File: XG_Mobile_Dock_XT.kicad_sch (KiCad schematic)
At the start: 45 parts, among them J1 5-1775443-8, J13 39301240, J14 I2C1, J2 20455-040E-76, J3 20455-040E-76, J5 USB_C_Receptacle, J6 455860005, J7 10147430-113T0LF, SW1 SW_Push

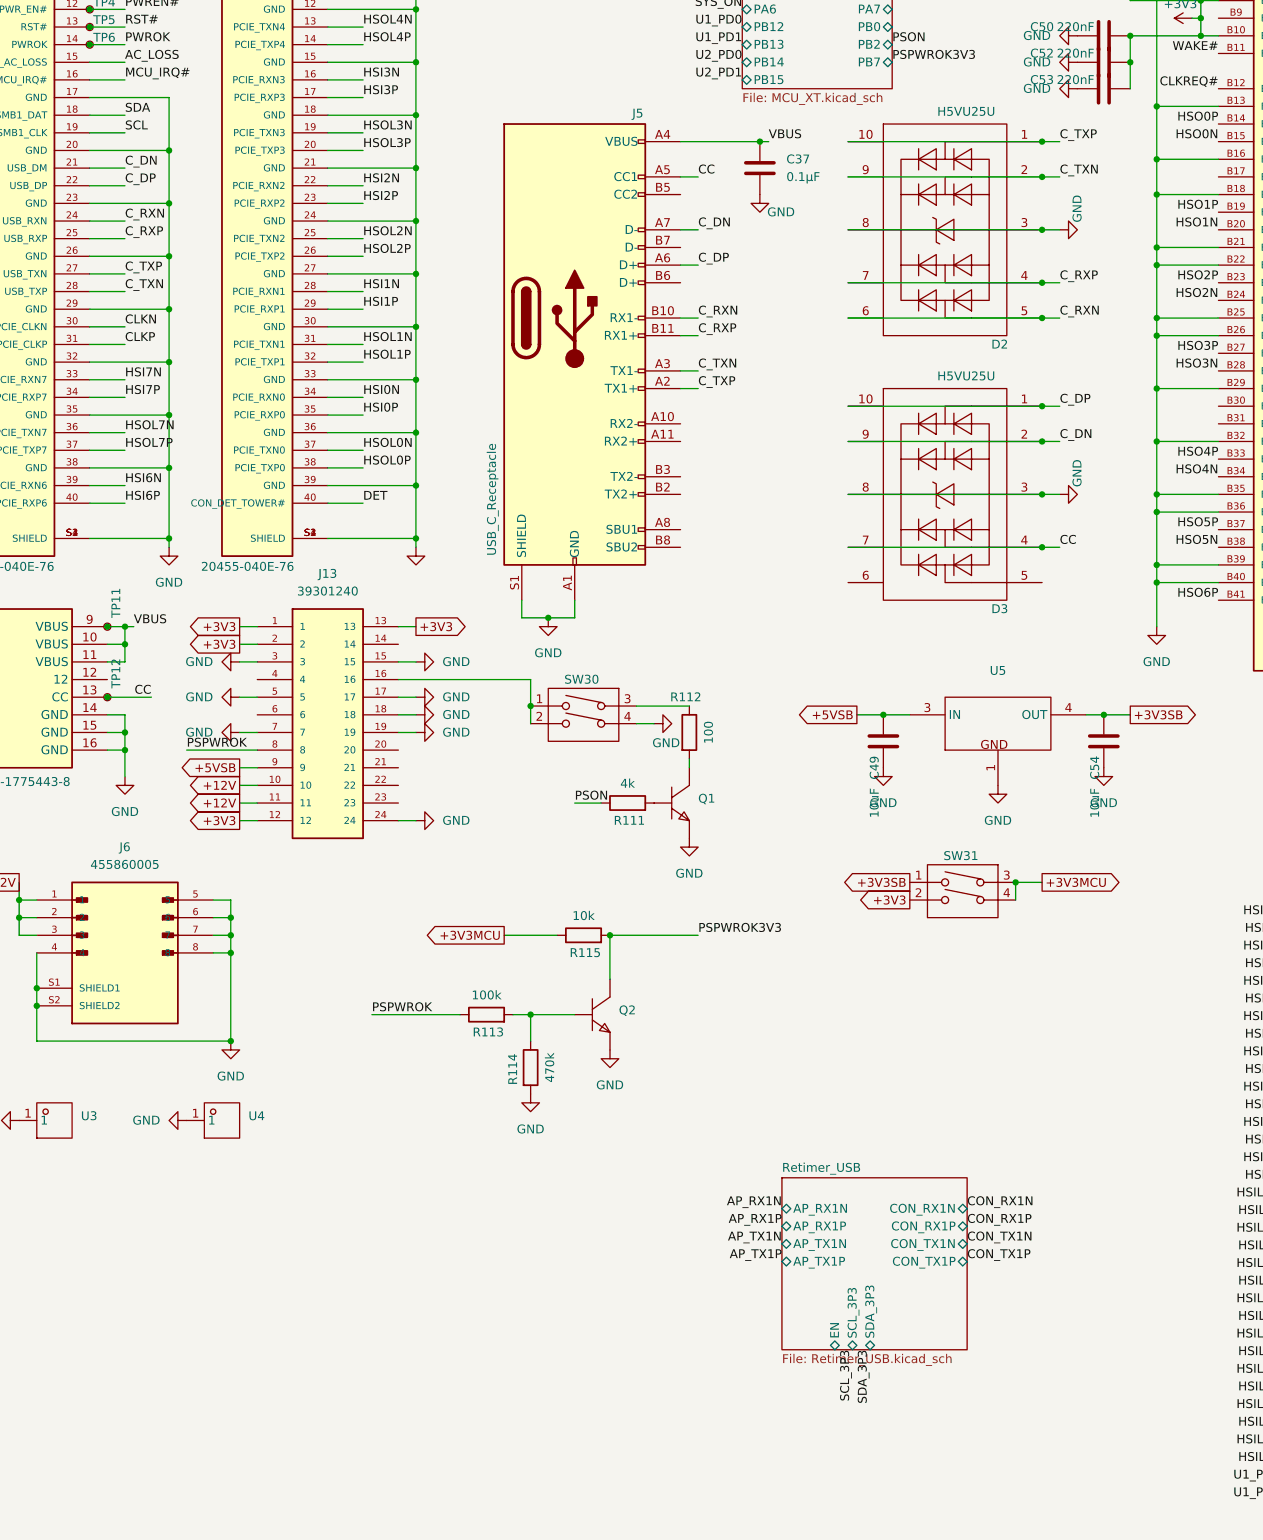
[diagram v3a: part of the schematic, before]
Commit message: almost finished adding retimer for usb
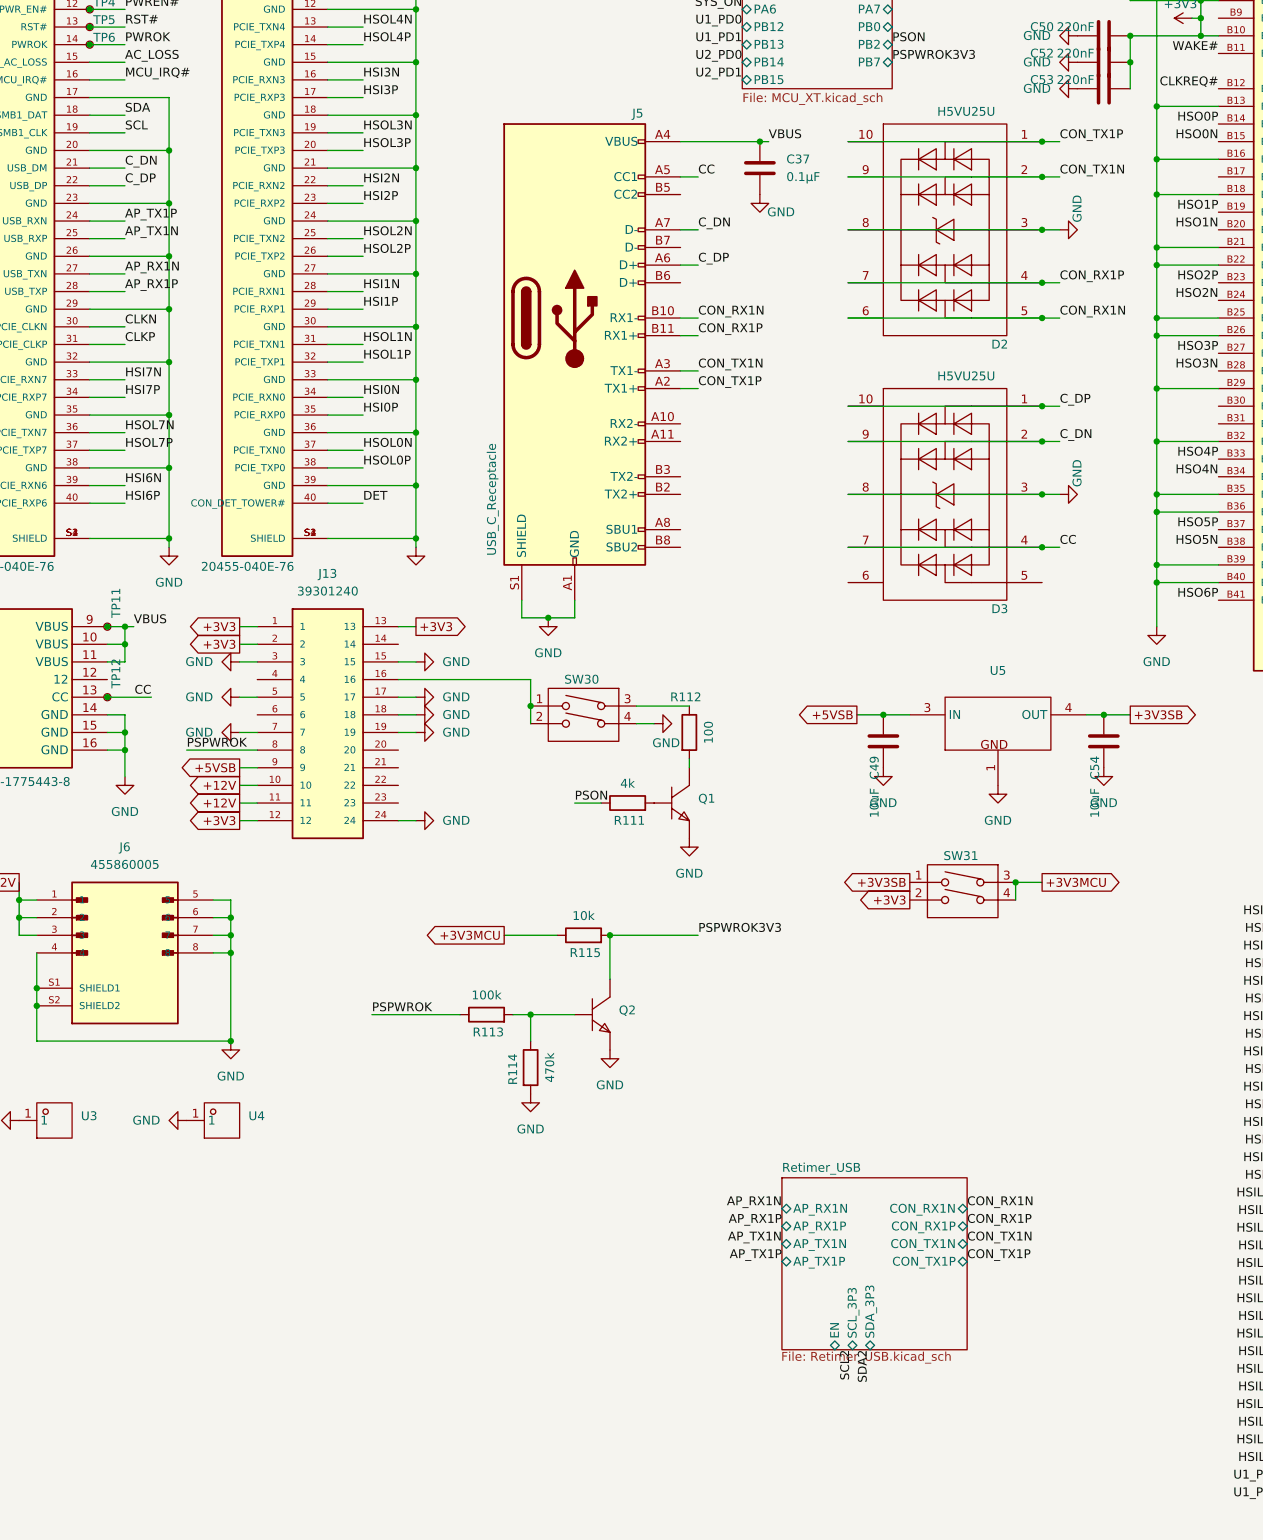
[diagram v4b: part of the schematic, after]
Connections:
- net AP_RX1N: now also J3.27 (USB_TXN)
- net AP_RX1P: now also J3.28 (USB_TXP)
- net AP_TX1N: now also J3.25 (USB_RXP)
- net AP_TX1P: now also J3.24 (USB_RXN)
- net CON_RX1N: now also D2.5 (I/O_4), D2.6 (NC), J5.B10 (RX1-)
- net CON_RX1P: now also D2.4 (I/O_3), D2.7 (NC), J5.B11 (RX1+)
- net CON_TX1N: now also D2.2 (I/O_2), D2.9 (NC), J5.A3 (TX1-)
- net CON_TX1P: now also D2.1 (I/O_1), D2.10 (NC), J5.A2 (TX1+)
- removed net C_RXN: D2.5 (I/O_4), D2.6 (NC), J3.24 (USB_RXN), J5.B10 (RX1-)
- removed net C_RXP: D2.4 (I/O_3), D2.7 (NC), J3.25 (USB_RXP), J5.B11 (RX1+)
- removed net C_TXN: D2.2 (I/O_2), D2.9 (NC), J3.28 (USB_TXP), J5.A3 (TX1-)
- removed net C_TXP: D2.1 (I/O_1), D2.10 (NC), J3.27 (USB_TXN), J5.A2 (TX1+)
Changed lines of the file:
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@@
 		)
 	)
-	(label "C_RXN"
+	(label "CON_RX1N"
 		(at 175.26 91.44 0)
 		(effects
@@
 		)
 	)
-	(label "C_RXN"
+	(label "CON_RX1N"
 		(at 123.19 91.44 0)
 		(effects
@@
 		)
 	)
-	(label "C_TXN"
+	(label "AP_RX1P"
 		(at 40.64 87.63 0)
 		(effects
@@
 		)
 	)
-	(label "C_TXP"
+	(label "CON_TX1P"
 		(at 175.26 66.04 0)
 		(effects
@@
 		)
 	)
-	(label "C_RXN"
+	(label "AP_TX1P"
 		(at 40.64 77.47 0)
 		(effects
@@
 		)
 	)
-	(label "C_RXP"
+	(label "AP_TX1N"
 		(at 40.64 80.01 0)
 		(effects
@@
 		)
 	)
-	(label "SDA_3P3"
+	(label "SDA2"
 		(at 147.955 240.03 270)
 		(effects
@@
 		)
 	)
-	(label "C_RXP"
+	(label "CON_RX1P"
 		(at 175.26 86.36 0)
 		(effects
@@
 		)
 	)
-	(label "C_TXP"
+	(label "CON_TX1P"
 		(at 123.19 101.6 0)
 		(effects
@@
 		)
 	)
-	(label "C_TXN"
+	(label "CON_TX1N"
 		(at 123.19 99.06 0)
 		(effects
@@
 		)
 	)
-	(label "C_TXN"
+	(label "CON_TX1N"
 		(at 175.26 71.12 0)
 		(effects
@@
 		)
 	)
-	(label "C_TXP"
+	(label "AP_RX1N"
 		(at 40.64 85.09 0)
 		(effects
@@
 		)
 	)
-	(label "C_RXP"
+	(label "CON_RX1P"
 		(at 123.19 93.98 0)
 		(effects
@@
 		)
 	)
-	(label "SCL_3P3"
+	(label "SCL2"
 		(at 145.415 240.03 270)
 		(effects
@@
 		(on_board yes)
 		(dnp no)
-		(fields_autoplaced yes)
 		(stroke
 			(width 0.1524)
@@
 		)
 		(property "Sheetfile" "Retimer_USB.kicad_sch"
-			(at 135.255 240.6146 0)
+			(at 135.128 240.284 0)
 			(effects
 				(font

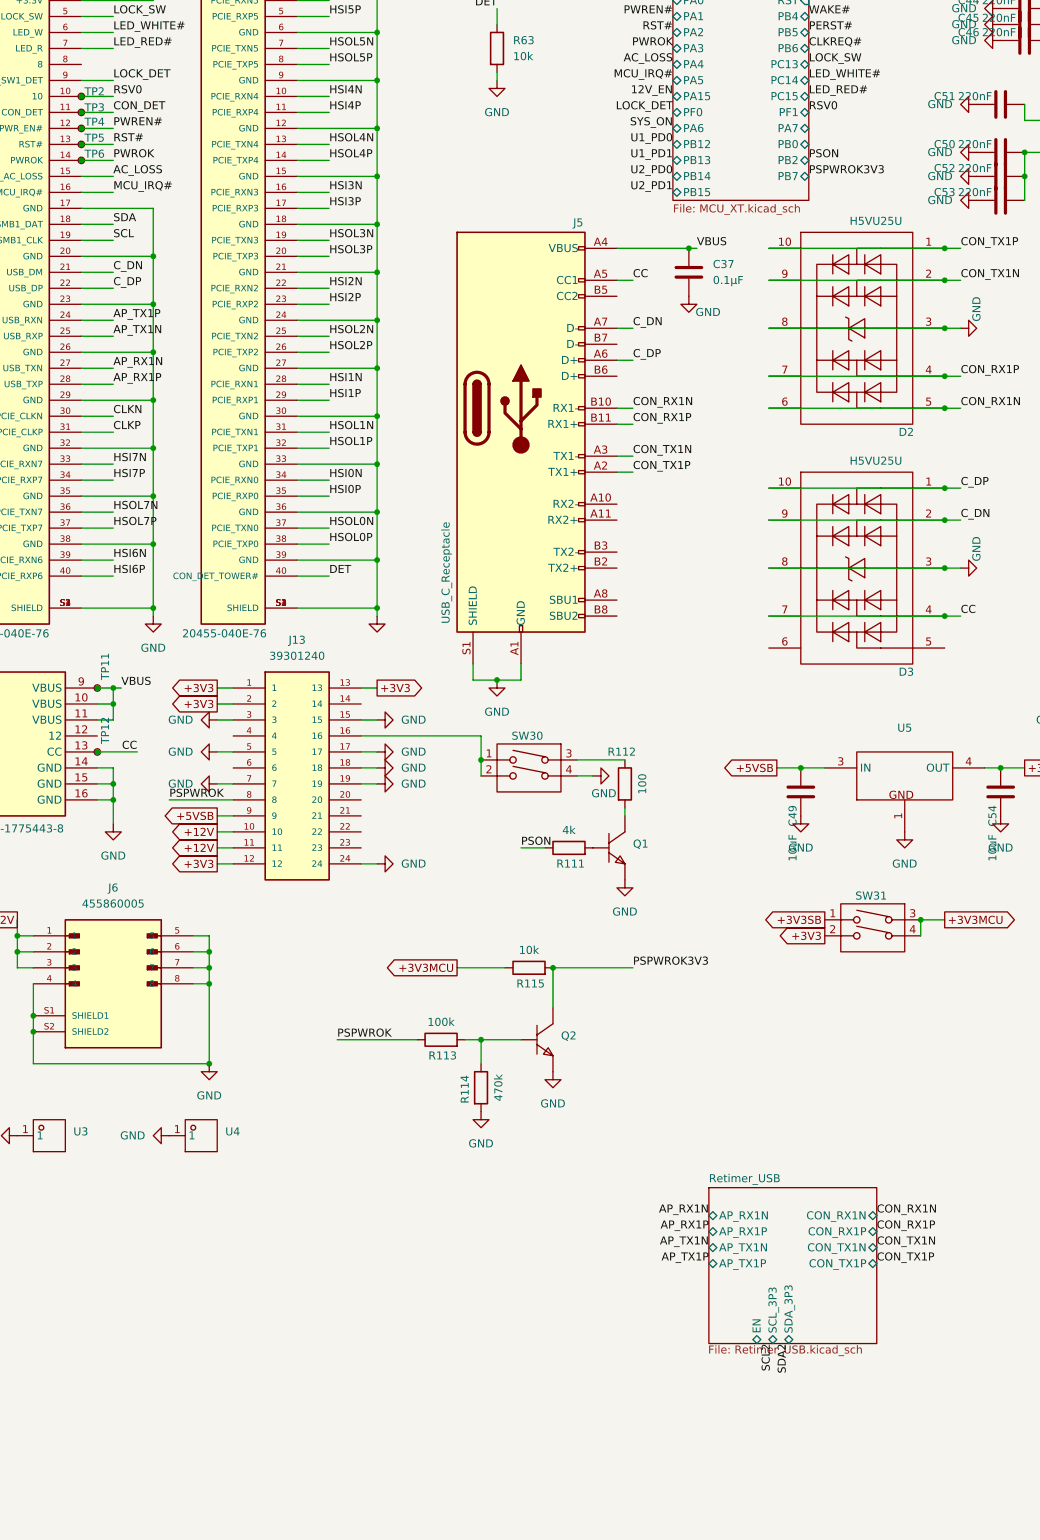
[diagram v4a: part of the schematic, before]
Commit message: almost finished with implementing usb retimer
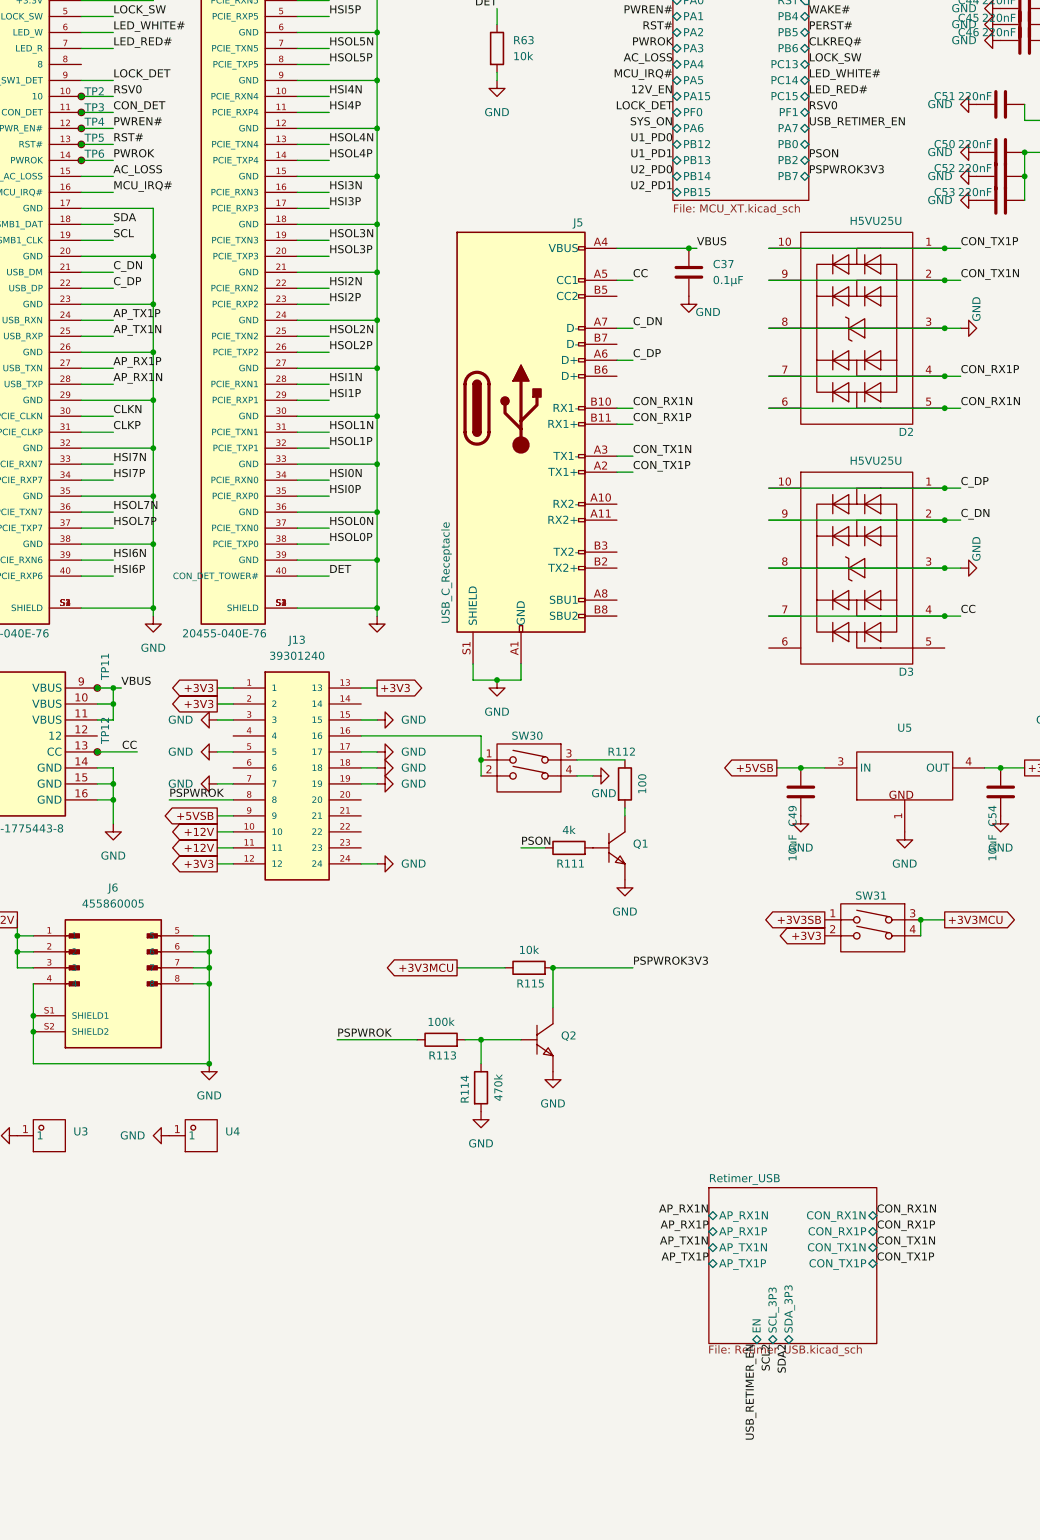
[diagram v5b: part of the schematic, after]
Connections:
- net AP_RX1N: now also J3.28 (USB_TXP); no longer J3.27 (USB_TXN)
- net AP_RX1P: now also J3.27 (USB_TXN); no longer J3.28 (USB_TXP)
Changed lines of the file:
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@@
+		)
+	)
+	(label "USB_RETIMER_EN"
+		(at 142.875 240.03 270)
+		(effects
+			(font
+				(size 1.27 1.27)
+			)
+			(justify right bottom)
 		)
 	)
@@
 	)
 	(label "AP_RX1P"
-		(at 40.64 87.63 0)
+		(at 40.64 85.09 0)
 		(effects
 			(font
@@
 		)
 	)
+	(label "USB_RETIMER_EN"
+		(at 151.13 46.99 0)
+		(effects
+			(font
+				(size 1.27 1.27)
+			)
+			(justify left bottom)
+		)
+	)
 	(label "HSI6P"
 		(at 40.64 118.11 0)
@@
 	)
 	(label "AP_RX1N"
-		(at 40.64 85.09 0)
-		(effects
-			(font
+		(at 40.64 87.63 0)
+		(effects
+			(font

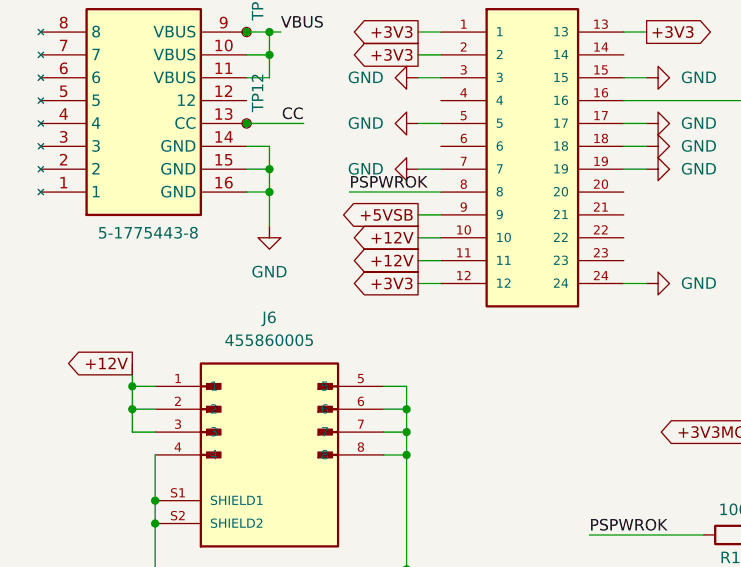
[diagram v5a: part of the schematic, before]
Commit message: added more power rails on new layers
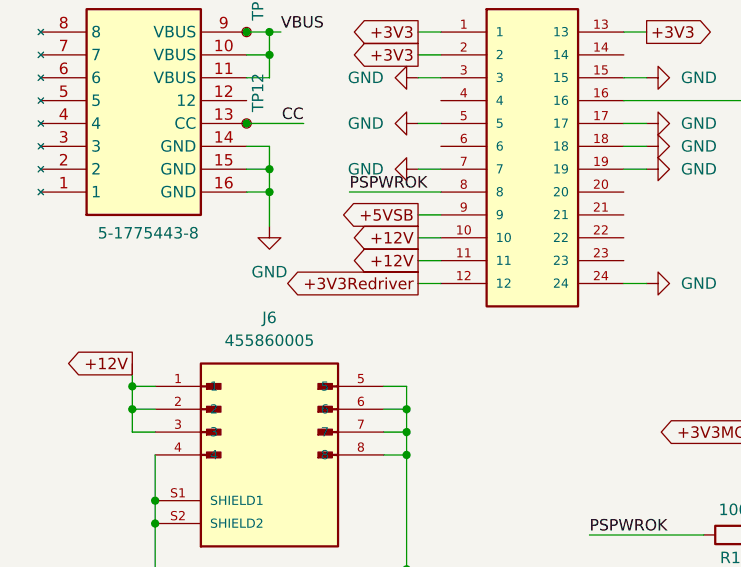
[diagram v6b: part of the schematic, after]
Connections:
- net +3V3: no longer J13.12
- new net +3V3Redriver: J13.12
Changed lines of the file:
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@@
 		)
 	)
-	(global_label "+3V3"
+	(global_label "+3V3Redriver"
 		(shape output)
 		(at 57.15 163.83 180)
@@
 		)
 		(property "Intersheetrefs" "${INTERSHEET_REFS}"
-			(at 49.0848 163.83 0)
+			(at 41.3438 163.83 0)
 			(effects
 				(font
